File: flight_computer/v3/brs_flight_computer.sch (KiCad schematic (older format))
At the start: 0 parts

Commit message: Updating based on harnesses
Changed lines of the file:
@@
 F9 "SCL" I L 4600 1450 50
 F10 "GAAS_TEMP" I L 4600 1350 50
-F11 "MUX_RESET" I L 4600 1050 50
-F12 "MUX_ENABLE" I L 4600 950 50
 $EndSheet
 Wire Wire Line
@@
 F23 "NC_V" I R 3750 6150 50
 F24 "READ_BUSS" I R 3750 4900 50
-F25 "MUX_ENABLE" I R 3750 950 50
-F26 "MUX_RESET" I R 3750 1050 50
 $EndSheet
-Wire Wire Line
-	4600 1050 3750 1050
-Wire Wire Line
-	3750 950  4600 950
 $EndSCHEMATC

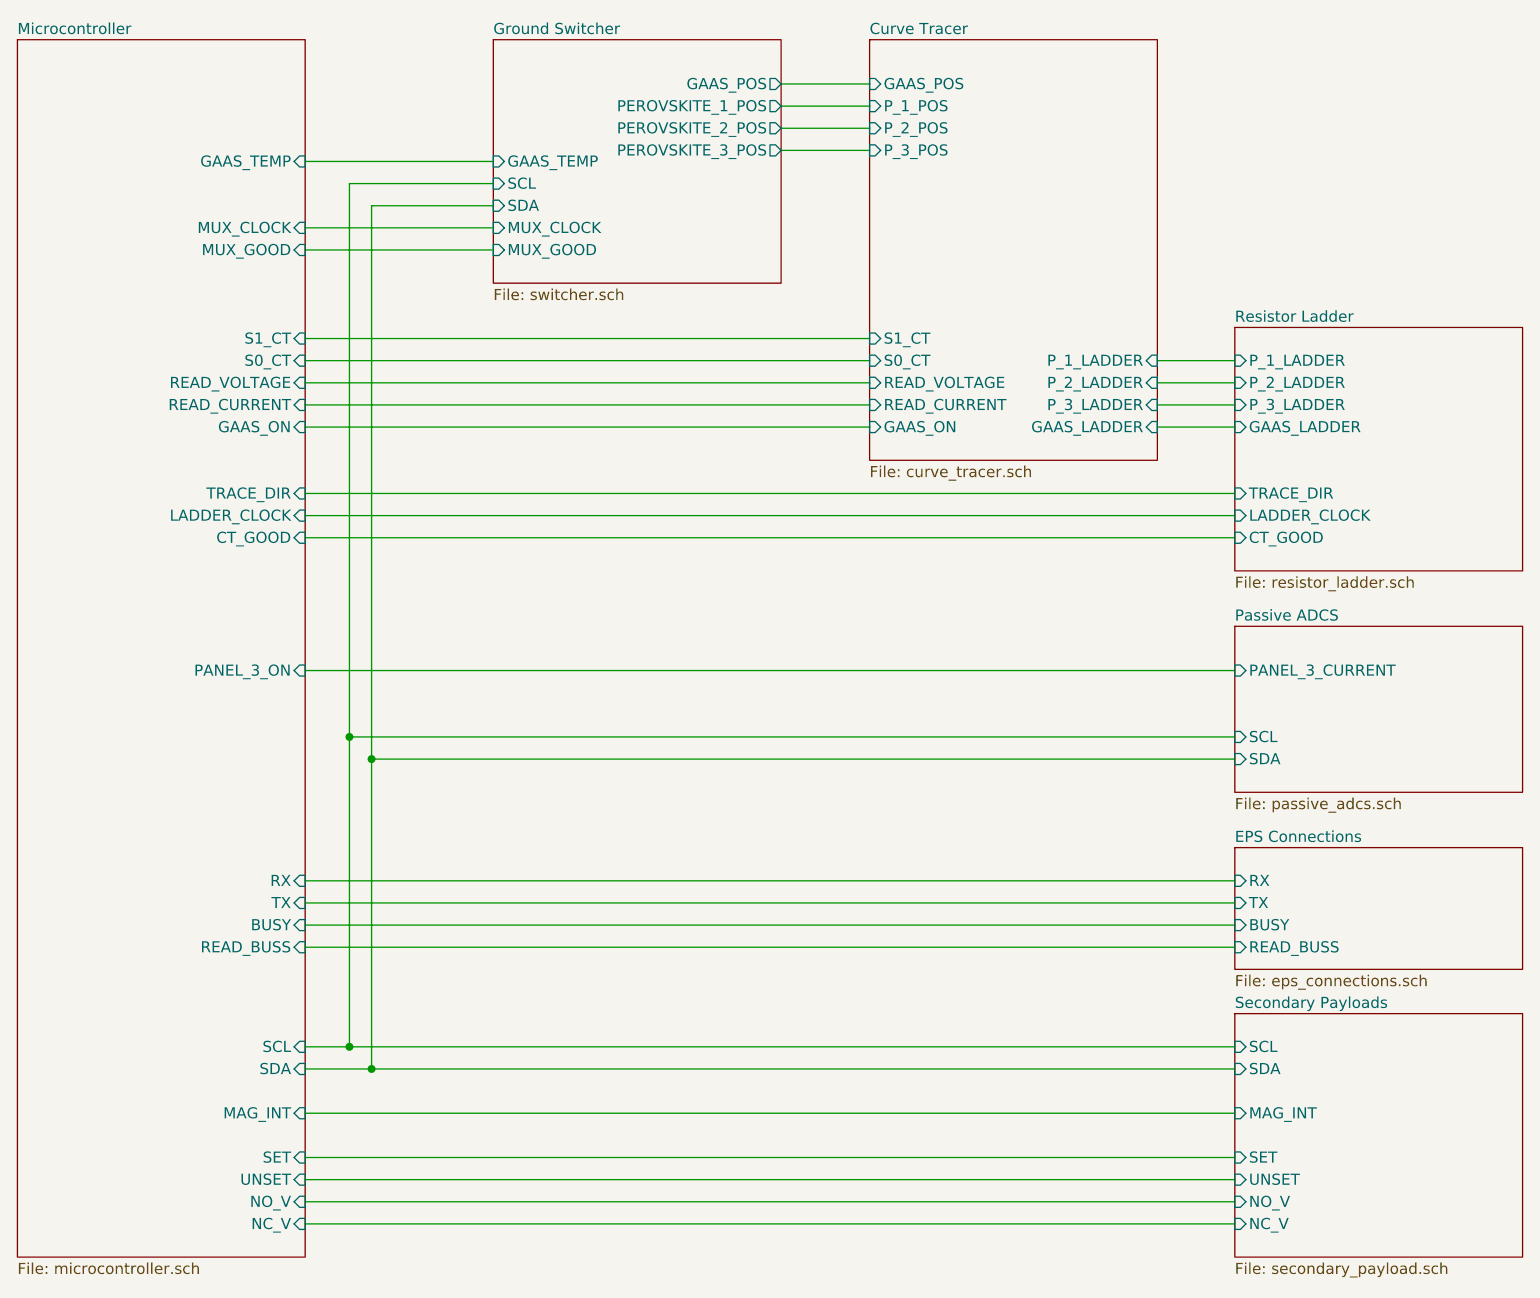
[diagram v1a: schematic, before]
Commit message: Update hardware
- Add separate discharge resistance paths to flight computer
- Update footprint for payload holder
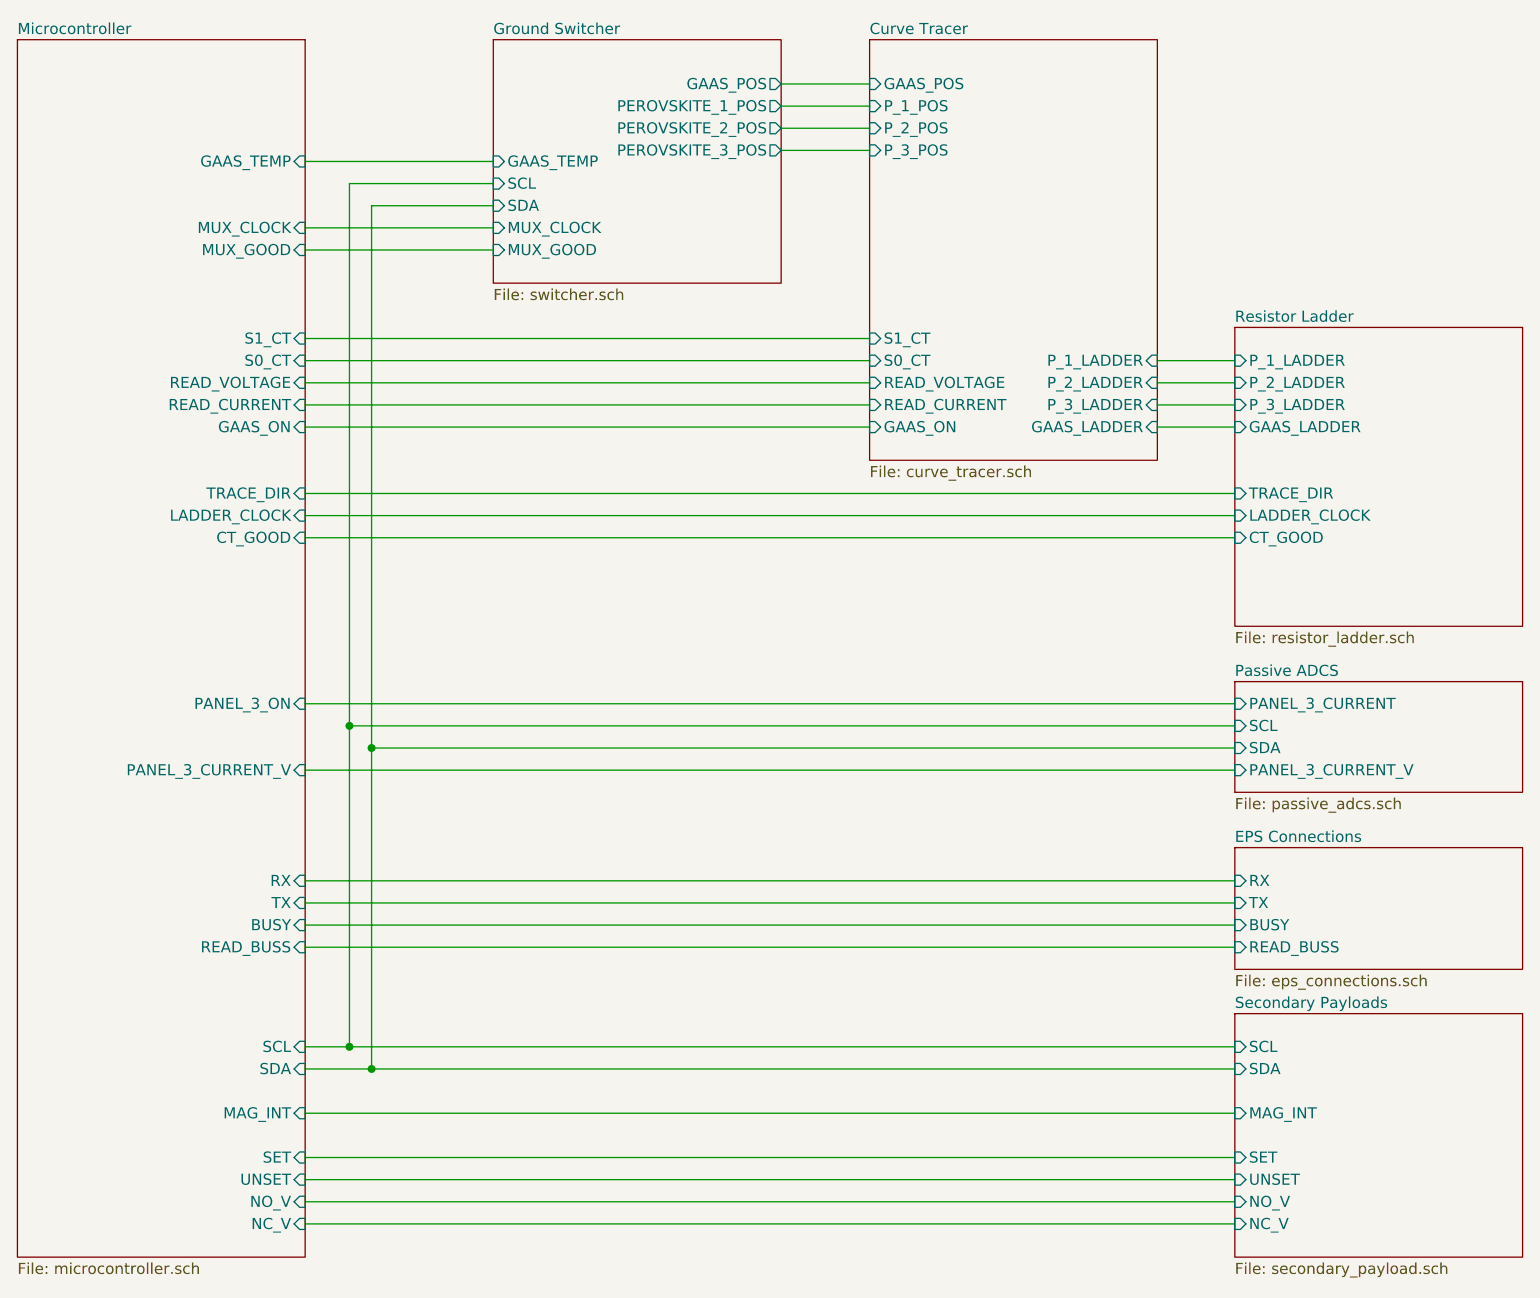
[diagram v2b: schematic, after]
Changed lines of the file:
@@
 $EndSheet
 $Sheet
-S 7950 3450 1300 750
+S 7950 3700 1300 500
 U 64D823E8
 F0 "Passive ADCS" 50
 F1 "passive_adcs.sch" 50
-F2 "PANEL_3_CURRENT" I L 7950 3650 50
-F3 "SCL" I L 7950 3950 50
-F4 "SDA" I L 7950 4050 50
+F2 "PANEL_3_CURRENT" I L 7950 3800 50
+F3 "SCL" I L 7950 3900 50
+F4 "SDA" I L 7950 4000 50
+F5 "PANEL_3_CURRENT_V" I L 7950 4100 50
 $EndSheet
 $Sheet
-S 7950 2100 1300 1100
+S 7950 2100 1300 1350
 U 64D82674
 F0 "Resistor Ladder" 50
@@
 	7950 3050 3750 3050
 Wire Wire Line
-	3750 3650 7950 3650
+	3750 3800 7950 3800
 Wire Wire Line
 	3750 4600 7950 4600
@@
 	4600 1550 4050 1550
 Wire Wire Line
-	4050 1550 4050 4050
+	4050 1550 4050 4000
 Connection ~ 4050 5450
 Wire Wire Line
 	4050 5450 3750 5450
 Wire Wire Line
-	7950 3950 3950 3950
+	7950 3900 3950 3900
 Wire Wire Line
-	3950 1450 3950 3950
-Connection ~ 3950 3950
+	3950 1450 3950 3900
 Wire Wire Line
-	3950 3950 3950 5350
-Wire Wire Line
-	7950 4050 4050 4050
-Connection ~ 4050 4050
-Wire Wire Line
-	4050 4050 4050 5450
+	7950 4000 4050 4000
 Wire Wire Line
 	7950 5850 3750 5850
@@
 F11 "TRACE_DIR" I R 3750 2850 50
 F12 "CT_GOOD" I R 3750 3050 50
-F13 "PANEL_3_ON" I R 3750 3650 50
+F13 "PANEL_3_ON" I R 3750 3800 50
 F14 "SCL" I R 3750 5350 50
 F15 "SDA" I R 3750 5450 50
@@
 F23 "NC_V" I R 3750 6150 50
 F24 "READ_BUSS" I R 3750 4900 50
+F25 "PANEL_3_CURRENT_V" I R 3750 4100 50
 $EndSheet
+Connection ~ 3950 3900
+Connection ~ 4050 4000
+Wire Wire Line
+	3950 3900 3950 5350
+Wire Wire Line
+	4050 4000 4050 5450
+Wire Wire Line
+	7950 4100 3750 4100
 $EndSCHEMATC
